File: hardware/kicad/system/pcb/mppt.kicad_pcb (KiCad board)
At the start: 2 copper layers, 164 x 82 mm, 21 parts, among them J1 PV ind, J2 til lager (V3), J3 sense -> Arduino, Q1 BD139, U1 LM358

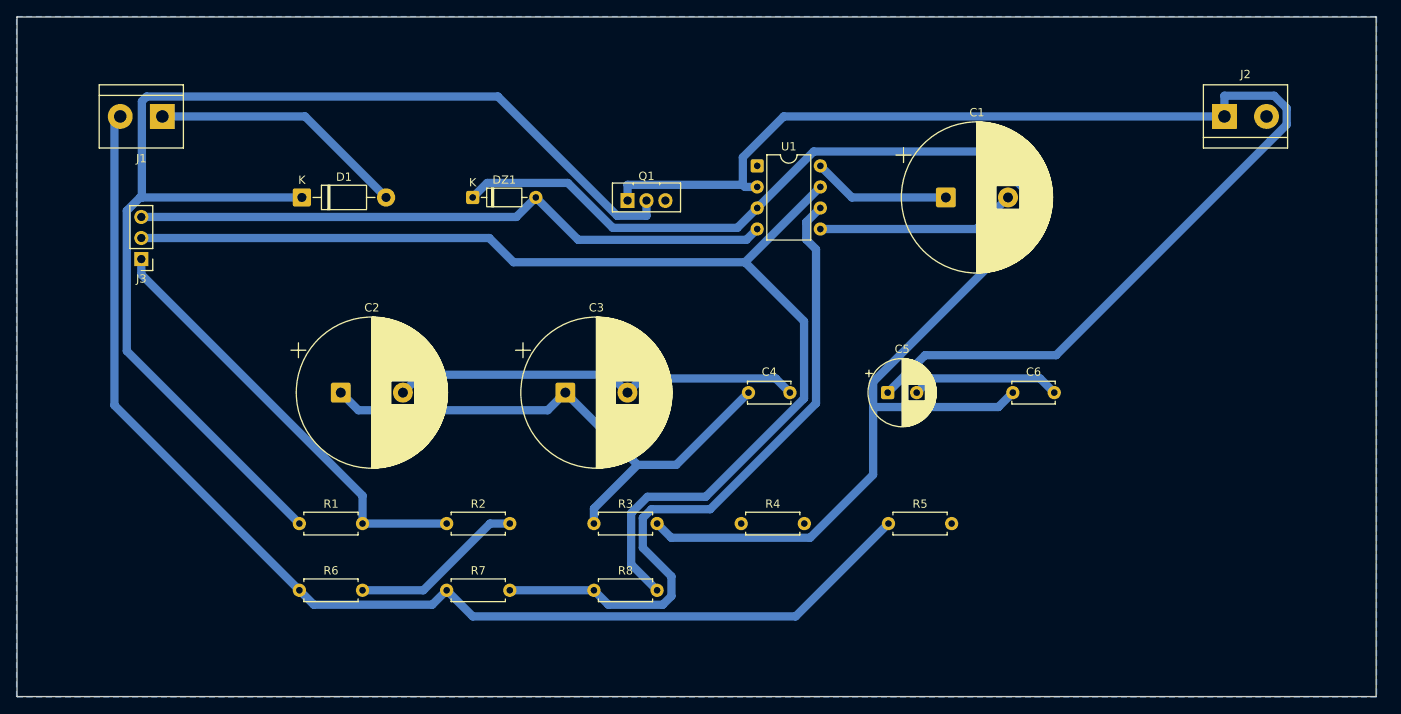
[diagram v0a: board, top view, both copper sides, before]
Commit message: Apply fiber-laser design rules from the DTU-PCB-prototyping guide
All seven boards rebuilt to meet the XTool fiber laser workflow
(SimsesLab/DTU-PCB-prototyping): 1.0 mm tracks, 0.8 mm clearance, solid
no-net fill zone on B.Cu (pad connection: none) so the laser only
engraves the isolation channels, DIP footprints switched to the
_LongPads variants from the guide's shop table.

TO packages cannot meet 0.8 mm pad-to-pad at stock sizes, so
energy_system.pretty now has TO-220-3_Vertical_LaserPads (pads narrowed
to 1.7 mm -> 0.84 mm gap; make_laserpads.py regenerates). The MPPT pass
transistor moves BD139 -> TIP41A (shop part): TO-126's 2.28 mm pitch can
never satisfy the rule, and TO-220 handles the ~7 W better anyway.

Two more bugs caught in this pass:
- Device:Q_NMOS uses letter pin numbers (G/D/S) while TO-220 pads are
  1/2/3 - buck/boost MOSFET pads silently got NO net in the earlier
  boards (no-net pads don't count as unconnected). pcb_build.py now maps
  G/D/S->1/2/3 and fails hard if a component ends up netless.
- DRC now 0 violations on all seven boards; remaining airwires are the
  documented jumpers.
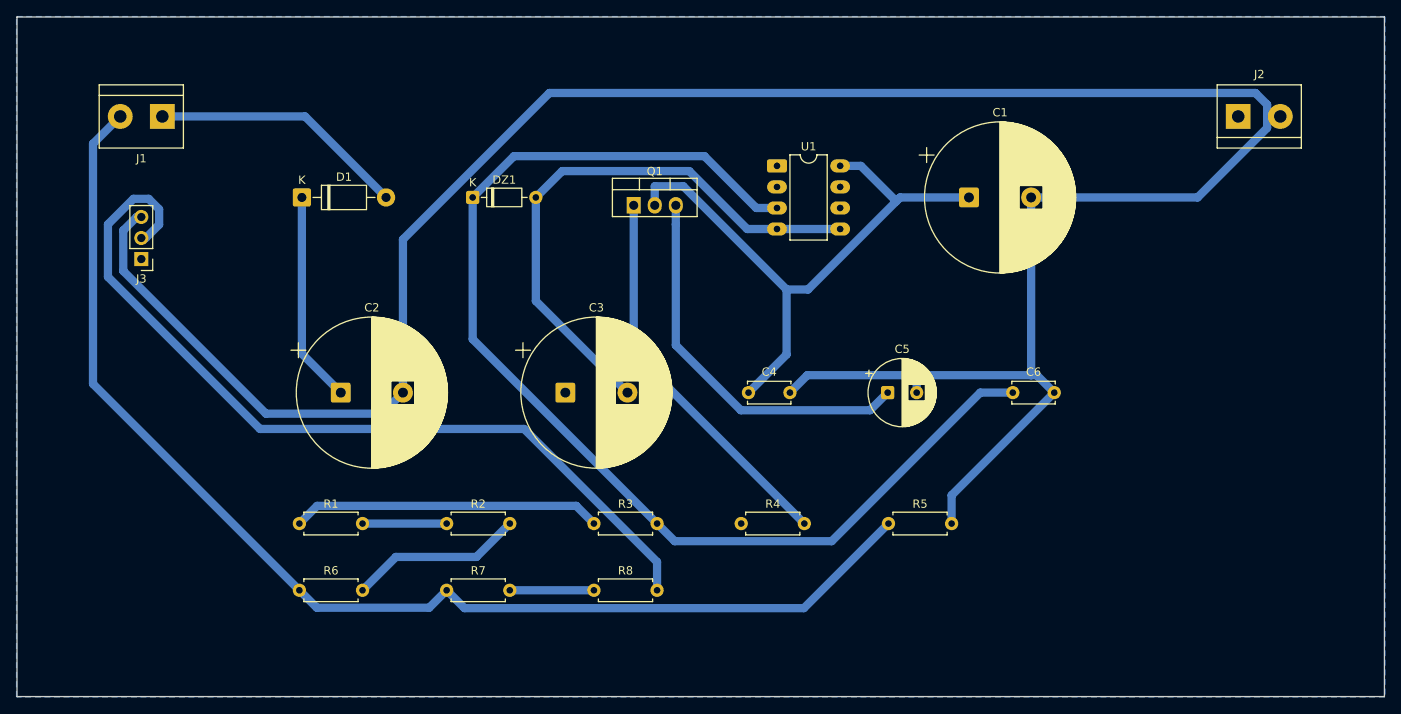
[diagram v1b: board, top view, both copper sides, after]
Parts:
- Q1: value BD139 -> TIP41A; footprint TO-126-3_Vertical -> TO-220-3_Vertical_LaserPads
- U1: footprint DIP-8_W7.62mm -> DIP-8_W7.62mm_LongPads
- moved C1 2.79 mm to (134.9, 41.8)
- moved U1 2.39 mm to (111.7, 38.0)
- moved J2 1.66 mm to (167.4, 32.0)
- moved Q1 0.94 mm to (94.4, 42.7)
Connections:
- Q1 pad 1: /V3_OUT -> /Q1_B
- Q1 pad 3: /Q1_B -> /V3_OUT
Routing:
- net GND: track 191.2 -> 385.0 mm
- net /V3_OUT: track 155.3 -> 46.6 mm
- net /PV_BUS: track 232.8 -> 135.7 mm
- net /U1B_FB: track 82.9 -> 10.1 mm
- net /Q1_B: track 0.00 -> 46.9 mm
- net /PV_V: track 53.1 -> 10.1 mm
- net /PV_I: track 143.5 -> 102.9 mm
- net /VREF: track 164.9 -> 141.2 mm
- net /PV_RET: track 145.2 -> 146.8 mm
- added copper zone on B.Cu, net (none)
- removed copper zone on B.Cu, net GND
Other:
- board size 164 x 82 mm -> 165 x 82 mm

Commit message: Engrave component references into the copper on all boards
The fiber laser has no silkscreen step, so the refdes (R1, U1, ...) are
placed as mirrored copper text on B.Cu next to each component - they
engrave in the same run as the traces and read correctly from the
solder side. Placement is collision-checked against tracks/pads/other
text (copper text over a track would short or sever it); tracks are
sampled into small boxes so diagonal runs don't false-positive. 86 of
96 labels fit; the handful dropped in dense spots are listed in
production/README.md and still appear on the F_Fab plots.

Also exports <board>_silk_top.dxf (F.Silkscreen + outline) per board as
an optional top-side engraving pass - run it on the component side
BEFORE the copper run, and do NOT mirror that one.

DRC still 0 violations on all seven; jumper lists updated.
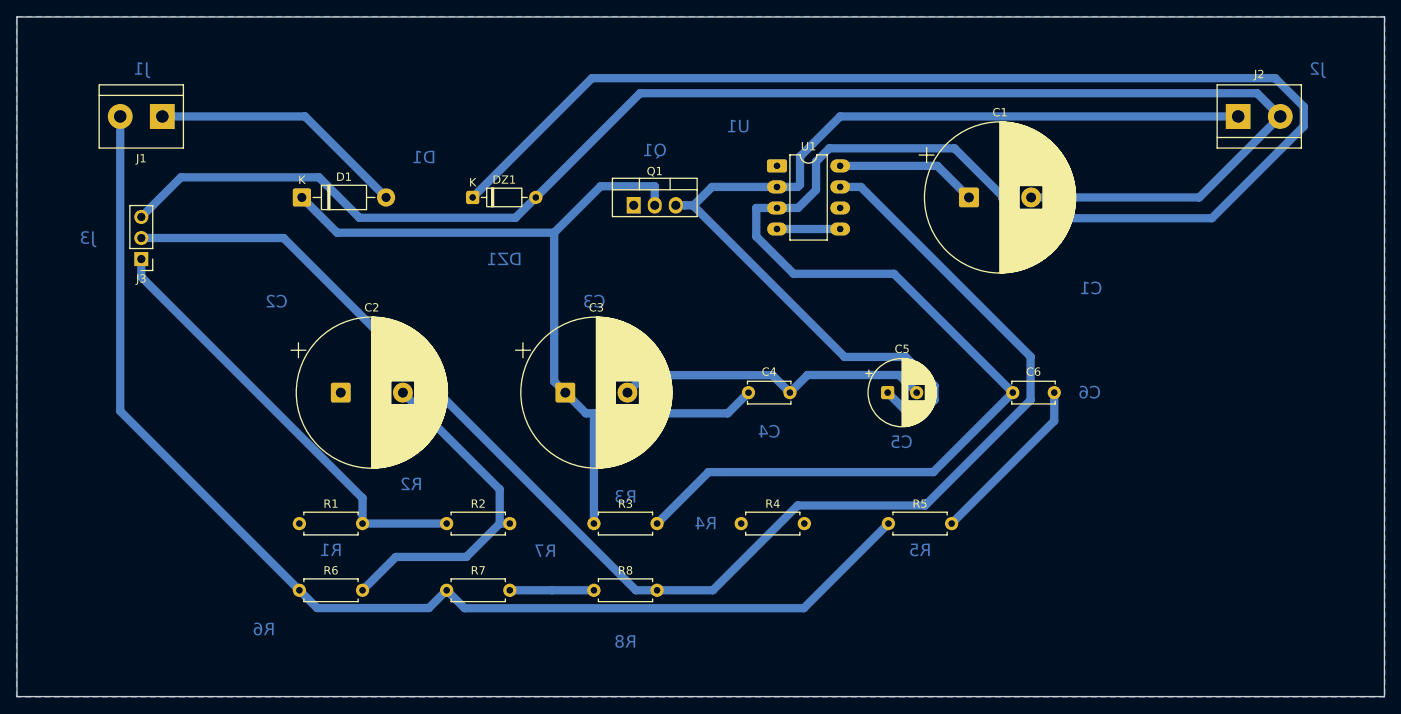
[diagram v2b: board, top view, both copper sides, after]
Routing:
- net /VREF: track 141.2 -> 281.0 mm
- net GND: track 385.0 -> 291.6 mm
- net /V3_OUT: track 46.6 -> 121.2 mm
- net /PV_I: track 102.9 -> 171.1 mm
- net /Q1_B: track 46.9 -> 0.00 mm
- net /PV_V: track 10.1 -> 53.1 mm
- net /PV_BUS: track 135.7 -> 123.4 mm
- net /PV_RET: track 146.8 -> 144.1 mm
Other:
- board text added: "C1"
- board text added: "C2"
- board text added: "C3"
- board text added: "C4"
- board text added: "C5"
- board text added: "C6"
- board text added: "D1"
- board text added: "DZ1"
- board text added: "J1"
- board text added: "J2"
- board text added: "J3"
- board text added: "Q1"
- board text added: "R1"
- board text added: "R2"
- board text added: "R3"
- board text added: "R4"
- board text added: "R5"
- board text added: "R6"
- board text added: "R7"
- board text added: "R8"
- board text added: "U1"
